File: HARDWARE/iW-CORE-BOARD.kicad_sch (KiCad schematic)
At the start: 0 parts

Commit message: Update first version of schematic
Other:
- added sheet DISPLAY (DISPLAY.kicad_sch)
- added sheet JTAG (JTAG.kicad_sch)
- added sheet POWER (POWER.kicad_sch)
- added sheet SDCARD (SDCARD.kicad_sch)
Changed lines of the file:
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@@
 	(paper "A4")
+	(sheet
+		(at 133.35 53.34)
+		(size 38.1 33.02)
+		(exclude_from_sim no)
+		(in_bom yes)
+		(on_board yes)
+		(dnp no)
+		(fields_autoplaced yes)
+		(stroke
+			(width 0.1524)
+			(type solid)
+		)
+		(fill
+			(color 0 0 0 0.0000)
+		)
+		(property "Sheetname" "SDCARD"
+			(at 133.35 52.6284 0)
+			(effects
+				(font
+					(size 1.27 1.27)
+				)
+				(justify left bottom)
+			)
+		)
+		(property "Sheetfile" "SDCARD.kicad_sch"
+			(at 133.35 86.9446 0)
+			(effects
+				(font
+					(size 1.27 1.27)
+				)
+				(justify left top)
+			)
+		)
+		(instances
+			(project "iW-CORE-BOARD"
+				(path "/8e673f85-6c19-4236-92ba-1263b1e08ba7"
+					(page "4")
+				)
+			)
+		)
+	)
+	(sheet
+		(at 133.35 93.98)
+		(size 38.1 22.86)
+		(exclude_from_sim no)
+		(in_bom yes)
+		(on_board yes)
+		(dnp no)
+		(fields_autoplaced yes)
+		(stroke
+			(width 0.1524)
+			(type solid)
+		)
+		(fill
+			(color 0 0 0 0.0000)
+		)
+		(property "Sheetname" "JTAG"
+			(at 133.35 93.2684 0)
+			(effects
+				(font
+					(size 1.27 1.27)
+				)
+				(justify left bottom)
+			)
+		)
+		(property "Sheetfile" "JTAG.kicad_sch"
+			(at 133.35 117.4246 0)
+			(effects
+				(font
+					(size 1.27 1.27)
+				)
+				(justify left top)
+			)
+		)
+		(instances
+			(project "iW-CORE-BOARD"
+				(path "/8e673f85-6c19-4236-92ba-1263b1e08ba7"
+					(page "6")
+				)
+			)
+		)
+	)
+	(sheet
+		(at 180.34 53.34)
+		(size 34.29 33.02)
+		(exclude_from_sim no)
+		(in_bom yes)
+		(on_board yes)
+		(dnp no)
+		(fields_autoplaced yes)
+		(stroke
+			(width 0.1524)
+			(type solid)
+		)
+		(fill
+			(color 0 0 0 0.0000)
+		)
+		(property "Sheetname" "DISPLAY"
+			(at 180.34 52.6284 0)
+			(effects
+				(font
+					(size 1.27 1.27)
+				)
+				(justify left bottom)
+			)
+		)
+		(property "Sheetfile" "DISPLAY.kicad_sch"
+			(at 180.34 86.9446 0)
+			(effects
+				(font
+					(size 1.27 1.27)
+				)
+				(justify left top)
+			)
+		)
+		(instances
+			(project "iW-CORE-BOARD"
+				(path "/8e673f85-6c19-4236-92ba-1263b1e08ba7"
+					(page "5")
+				)
+			)
+		)
+	)
+	(sheet
+		(at 82.55 93.98)
+		(size 38.1 22.86)
+		(exclude_from_sim no)
+		(in_bom yes)
+		(on_board yes)
+		(dnp no)
+		(fields_autoplaced yes)
+		(stroke
+			(width 0.1524)
+			(type solid)
+		)
+		(fill
+			(color 0 0 0 0.0000)
+		)
+		(property "Sheetname" "POWER"
+			(at 82.55 93.2684 0)
+			(effects
+				(font
+					(size 1.27 1.27)
+				)
+				(justify left bottom)
+			)
+		)
+		(property "Sheetfile" "POWER.kicad_sch"
+			(at 82.55 117.4246 0)
+			(effects
+				(font
+					(size 1.27 1.27)
+				)
+				(justify left top)
+			)
+		)
+		(instances
+			(project "iW-CORE-BOARD"
+				(path "/8e673f85-6c19-4236-92ba-1263b1e08ba7"
+					(page "3")
+				)
+			)
+		)
+	)
 	(sheet
 		(at 82.55 53.34)

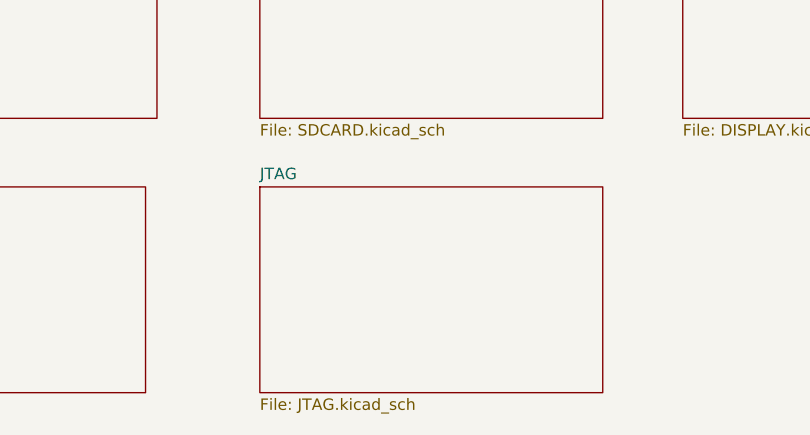
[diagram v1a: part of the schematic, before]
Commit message: fix fpc
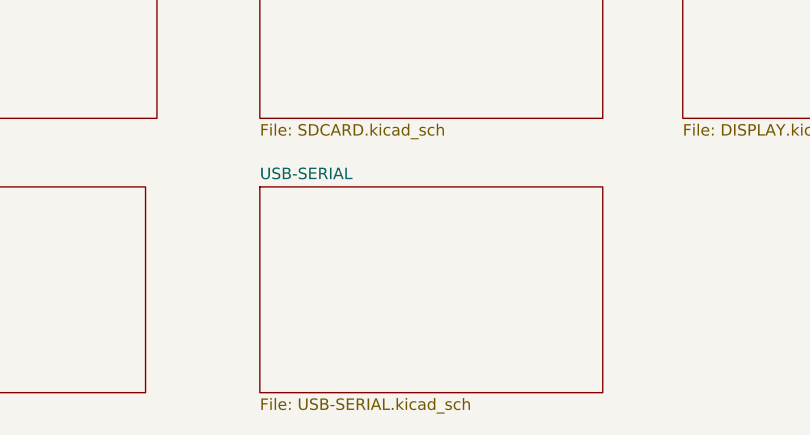
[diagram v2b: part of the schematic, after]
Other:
- removed sheet JTAG
- added sheet USB-SERIAL (USB-SERIAL.kicad_sch)
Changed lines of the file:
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@@
 			(color 0 0 0 0.0000)
 		)
-		(property "Sheetname" "JTAG"
+		(property "Sheetname" "USB-SERIAL"
 			(at 133.35 93.2684 0)
 			(effects
@@
 			)
 		)
-		(property "Sheetfile" "JTAG.kicad_sch"
+		(property "Sheetfile" "USB-SERIAL.kicad_sch"
 			(at 133.35 117.4246 0)
 			(effects
